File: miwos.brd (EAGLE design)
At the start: 120 x 120 mm, 44 parts, among them J1 614004190021, U1 PEC16, U3 PEC16

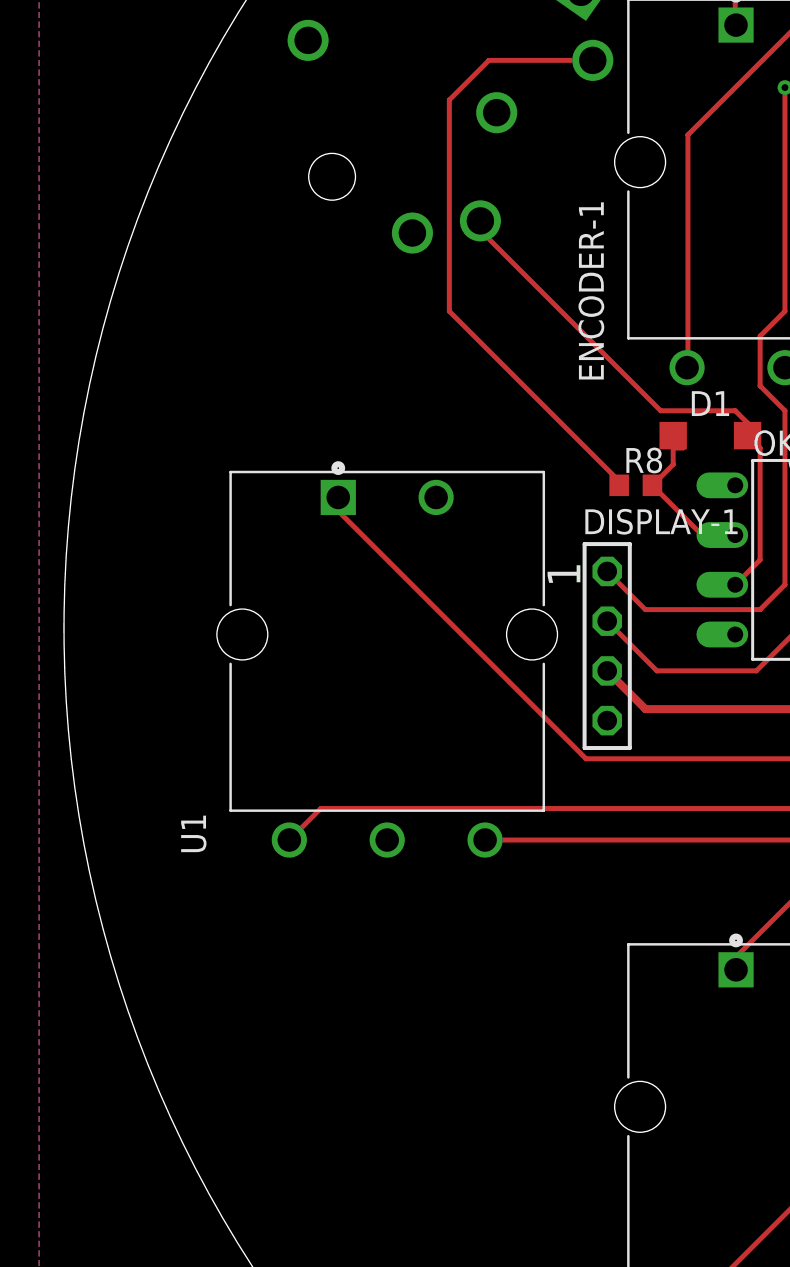
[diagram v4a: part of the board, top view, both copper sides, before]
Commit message: Add encoder LEDs, don't wire them for now
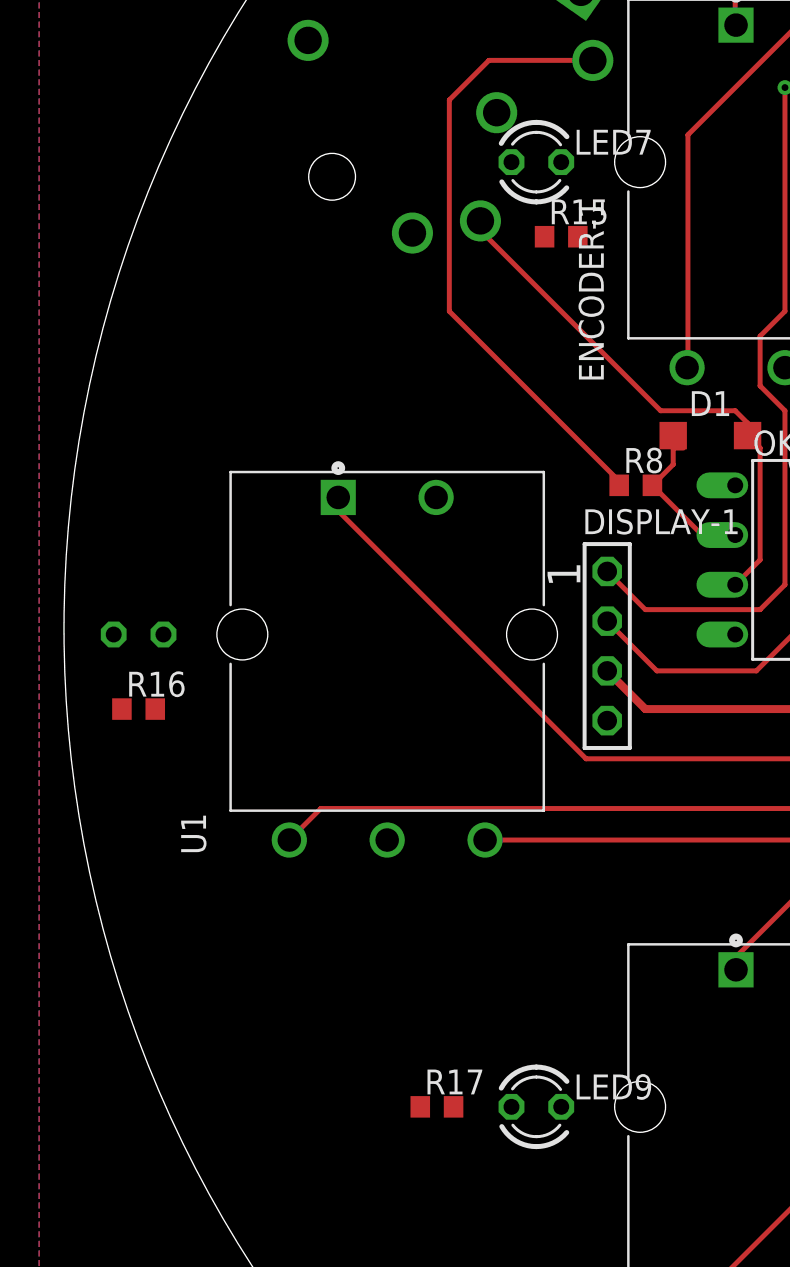
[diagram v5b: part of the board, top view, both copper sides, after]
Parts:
- added LED7, LED8, LED9: (no value), led:LED3MM
- added R15, R16, R17: 220R, rcl:R0603
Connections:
- new net ENCODER-1-LED: R15.1
- new net ENCODER-2-LED: R16.1
- new net ENCODER-3-LED: R17.1
- new net N$20: LED8.A, R16.2
- new net N$22: LED9.A, R17.2
- new net N$4: LED7.A, R15.2
- net GND: now also LED7.K, LED8.K, LED9.K
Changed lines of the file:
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@@
 <attribute name="VALUE" x="71.755" y="4.445" size="1.27" layer="27"/>
+</element>
+<element name="LED7" library="led" library_urn="urn:adsk.eagle:library:259" package="LED3MM" package3d_urn="urn:adsk.eagle:package:15797/1" value="" x="24.13" y="83.82" smashed="yes">
+<attribute name="NAME" x="26.035" y="84.201" size="1.27" layer="25" ratio="10"/>
+<attribute name="POPULARITY" value="97" x="24.13" y="90.17" size="1.778" layer="27" display="off"/>
+<attribute name="VALUE" x="26.035" y="82.169" size="1.27" layer="27" ratio="10"/>
+</element>
+<element name="R15" library="rcl" library_urn="urn:adsk.eagle:library:334" package="R0603" package3d_urn="urn:adsk.eagle:package:23555/3" value="220R" x="25.4" y="80.01" smashed="yes">
+<attribute name="NAME" x="24.765" y="80.645" size="1.27" layer="25"/>
+<attribute name="POPULARITY" value="70" x="25.4" y="76.2" size="1.778" layer="27" display="off"/>
+<attribute name="SPICEPREFIX" value="R" x="25.4" y="76.2" size="1.778" layer="27" display="off"/>
+<attribute name="VALUE" x="24.765" y="78.105" size="1.27" layer="27"/>
+</element>
+<element name="LED8" library="led" library_urn="urn:adsk.eagle:library:259" package="LED3MM" package3d_urn="urn:adsk.eagle:package:15797/1" value="" x="3.81" y="59.69" smashed="yes" rot="MR180">
+<attribute name="NAME" x="5.715" y="59.309" size="1.27" layer="26" ratio="10" rot="MR180"/>
+<attribute name="POPULARITY" value="97" x="3.81" y="54.61" size="1.778" layer="28" rot="MR180" display="off"/>
+<attribute name="VALUE" x="5.715" y="61.341" size="1.27" layer="28" ratio="10" rot="MR180"/>
+</element>
+<element name="R16" library="rcl" library_urn="urn:adsk.eagle:library:334" package="R0603" package3d_urn="urn:adsk.eagle:package:23555/3" value="220R" x="3.81" y="55.88" smashed="yes">
+<attribute name="NAME" x="3.175" y="56.515" size="1.27" layer="25"/>
+<attribute name="POPULARITY" value="70" x="3.81" y="50.8" size="1.778" layer="27" display="off"/>
+<attribute name="SPICEPREFIX" value="R" x="3.81" y="50.8" size="1.778" layer="27" display="off"/>
+<attribute name="VALUE" x="3.175" y="53.975" size="1.27" layer="27"/>
+</element>
+<element name="LED9" library="led" library_urn="urn:adsk.eagle:library:259" package="LED3MM" package3d_urn="urn:adsk.eagle:package:15797/1" value="" x="24.13" y="35.56" smashed="yes">
+<attribute name="NAME" x="26.035" y="35.941" size="1.27" layer="25" ratio="10"/>
+<attribute name="POPULARITY" value="97" x="24.13" y="40.64" size="1.778" layer="27" display="off"/>
+<attribute name="VALUE" x="26.035" y="33.909" size="1.27" layer="27" ratio="10"/>
+</element>
+<element name="R17" library="rcl" library_urn="urn:adsk.eagle:library:334" package="R0603" package3d_urn="urn:adsk.eagle:package:23555/3" value="220R" x="19.05" y="35.56" smashed="yes">
+<attribute name="NAME" x="18.415" y="36.195" size="1.27" layer="25"/>
+<attribute name="POPULARITY" value="70" x="19.05" y="30.48" size="1.778" layer="27" display="off"/>
+<attribute name="SPICEPREFIX" value="R" x="19.05" y="30.48" size="1.778" layer="27" display="off"/>
+<attribute name="VALUE" x="18.415" y="33.655" size="1.27" layer="27"/>
 </element>
 </elements>
@@
 <vertex x="-1.27" y="128.27"/>
 </polygon>
-<wire x1="91.44" y1="49.53" x2="41.91" y2="6.35" width="0" layer="19" extent="1-1"/>
-<wire x1="60.96" y1="6.35" x2="91.44" y2="49.53" width="0" layer="19" extent="1-1"/>
-<wire x1="78.74" y1="6.35" x2="60.96" y2="6.35" width="0" layer="19" extent="1-1"/>
-<wire x1="106.68" y1="74.93" x2="91.44" y2="49.53" width="0" layer="19" extent="1-1"/>
-<wire x1="101.6" y1="60.96" x2="106.68" y2="74.93" width="0" layer="19" extent="1-1"/>
-<wire x1="16.51" y1="49.19" x2="106.68" y2="74.93" width="0" layer="19" extent="1-1"/>
+<contactref element="LED7" pad="K"/>
+<contactref element="LED8" pad="K"/>
+<contactref element="LED9" pad="K"/>
+<wire x1="107.529703125" y1="90.04" x2="104.661821875" y2="94.135759375" width="0" layer="19" extent="1-1"/>
+<wire x1="97.89605" y1="86.34638125" x2="104.661821875" y2="94.135759375" width="0" layer="19" extent="1-1"/>
+<wire x1="97.75" y1="77.43" x2="97.89605" y2="86.34638125" width="0" layer="19" extent="1-1"/>
+<wire x1="97.75" y1="72.43" x2="97.75" y2="77.43" width="0" layer="19" extent="1-1"/>
+<wire x1="106.68" y1="74.93" x2="97.75" y2="77.43" width="0" layer="19" extent="1-1"/>
+<wire x1="92.67" y1="63.46" x2="97.75" y2="72.43" width="0" layer="19" extent="1-1"/>
+<wire x1="92.67" y1="58.46" x2="92.67" y2="63.46" width="0" layer="19" extent="1-1"/>
+<wire x1="91.44" y1="49.53" x2="92.67" y2="58.46" width="0" layer="19" extent="1-1"/>
+<wire x1="101.6" y1="60.96" x2="92.67" y2="63.46" width="0" layer="19" extent="1-1"/>
+<wire x1="105.9038" y1="56.8572" x2="101.6" y2="60.96" width="0" layer="19" extent="1-1"/>
+<wire x1="82.51" y1="52.03" x2="91.44" y2="49.53" width="0" layer="19" extent="1-1"/>
+<wire x1="82.51" y1="47.03" x2="82.51" y2="52.03" width="0" layer="19" extent="1-1"/>
+<wire x1="87.615503125" y1="108.8699" x2="104.661821875" y2="94.135759375" width="0" layer="19" extent="1-1"/>
+<wire x1="83.16046875" y1="111.13985" x2="87.615503125" y2="108.8699" width="0" layer="19" extent="1-1"/>
+<wire x1="67.31" y1="116.84" x2="83.16046875" y2="111.13985" width="0" layer="19" extent="1-1"/>
+<wire x1="64.31" y1="102.87" x2="67.31" y2="116.84" width="0" layer="19" extent="1-1"/>
+<wire x1="64.31" y1="100.33" x2="64.31" y2="102.87" width="0" layer="19" extent="1-1"/>
+<wire x1="73.66" y1="90.17" x2="64.31" y2="100.33" width="0" layer="19" extent="1-1"/>
+<wire x1="74.51" y1="80.01" x2="73.66" y2="90.17" width="0" layer="19" extent="1-1"/>
+<wire x1="39.1564625" y1="101.0859" x2="64.31" y2="100.33" width="0" layer="19" extent="1-1"/>
+<wire x1="39.33" y1="90.82" x2="39.1564625" y2="101.0859" width="0" layer="19" extent="1-1"/>
+<wire x1="36.839534375" y1="111.13985" x2="39.1564625" y2="101.0859" width="0" layer="19" extent="1-1"/>
+<wire x1="32.3845" y1="108.8699" x2="36.839534375" y2="111.13985" width="0" layer="19" extent="1-1"/>
+<wire x1="48.26" y1="80.01" x2="39.33" y2="90.82" width="0" layer="19" extent="1-1"/>
+<wire x1="44.03" y1="69.85" x2="48.26" y2="80.01" width="0" layer="19" extent="1-1"/>
+<wire x1="36.83" y1="73.32" x2="44.03" y2="69.85" width="0" layer="19" extent="1-1"/>
+<wire x1="41.91" y1="59.69" x2="44.03" y2="69.85" width="0" layer="19" extent="1-1"/>
+<wire x1="27.75" y1="55.29" x2="41.91" y2="59.69" width="0" layer="19" extent="1-1"/>
+<wire x1="16.51" y1="49.19" x2="27.75" y2="55.29" width="0" layer="19" extent="1-1"/>
+<wire x1="19.01" y1="66.69" x2="27.75" y2="55.29" width="0" layer="19" extent="1-1"/>
+<wire x1="39.33" y1="42.56" x2="27.75" y2="55.29" width="0" layer="19" extent="1-1"/>
+<wire x1="48.75" y1="32.62" x2="39.33" y2="42.56" width="0" layer="19" extent="1-1"/>
+<wire x1="36.83" y1="25.06" x2="48.75" y2="32.62" width="0" layer="19" extent="1-1"/>
+<wire x1="45.5" y1="18.5" x2="36.83" y2="25.06" width="0" layer="19" extent="1-1"/>
+<wire x1="45.5" y1="13.5" x2="45.5" y2="18.5" width="0" layer="19" extent="1-1"/>
+<wire x1="41.91" y1="6.35" x2="45.5" y2="13.5" width="0" layer="19" extent="1-1"/>
+<wire x1="62.5" y1="18.5" x2="45.5" y2="18.5" width="0" layer="19" extent="1-1"/>
+<wire x1="62.5" y1="13.5" x2="62.5" y2="18.5" width="0" layer="19" extent="1-1"/>
+<wire x1="60.96" y1="6.35" x2="62.5" y2="13.5" width="0" layer="19" extent="1-1"/>
+<wire x1="79.5" y1="18.5" x2="62.5" y2="18.5" width="0" layer="19" extent="1-1"/>
+<wire x1="79.5" y1="13.5" x2="79.5" y2="18.5" width="0" layer="19" extent="1-1"/>
+<wire x1="78.74" y1="6.35" x2="79.5" y2="13.5" width="0" layer="19" extent="1-1"/>
+<wire x1="15.33818125" y1="94.135759375" x2="32.3845" y2="108.8699" width="0" layer="19" extent="1-1"/>
+<wire x1="12.4703" y1="90.04" x2="15.33818125" y2="94.135759375" width="0" layer="19" extent="1-1"/>
+<wire x1="25.4" y1="83.82" x2="41.91" y2="6.35" width="0" layer="19" extent="1-1"/>
+<wire x1="5.08" y1="59.69" x2="25.4" y2="83.82" width="0" layer="19" extent="1-1"/>
+<wire x1="25.4" y1="35.56" x2="5.08" y2="59.69" width="0" layer="19" extent="1-1"/>
 </signal>
 <signal name="ENCODER-2-A">
@@
 <contactref element="TEENSY-41" pad="39"/>
 </signal>
+<signal name="N$4">
+<contactref element="LED7" pad="A"/>
+<contactref element="R15" pad="2"/>
+<wire x1="26.25" y1="80.01" x2="22.86" y2="83.82" width="0" layer="19" extent="1-1"/>
+</signal>
+<signal name="N$20">
+<contactref element="LED8" pad="A"/>
+<contactref element="R16" pad="2"/>
+<wire x1="4.66" y1="55.88" x2="2.54" y2="59.69" width="0" layer="19" extent="1-1"/>
+</signal>
+<signal name="N$22">
+<contactref element="LED9" pad="A"/>
+<contactref element="R17" pad="2"/>
+<wire x1="19.9" y1="35.56" x2="22.86" y2="35.56" width="0" layer="19" extent="1-1"/>
+</signal>
+<signal name="ENCODER-1-LED">
+<contactref element="R15" pad="1"/>
+</signal>
+<signal name="ENCODER-2-LED">
+<contactref element="R16" pad="1"/>
+</signal>
+<signal name="ENCODER-3-LED">
+<contactref element="R17" pad="1"/>
+</signal>
 </signals>
